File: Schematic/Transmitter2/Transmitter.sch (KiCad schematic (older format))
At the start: 50 parts, among them J1 Conn_01x06, J2 Antenna, J3 Conn_01x01, Q1 MMBT3904, Q2 MMBT3904, Q3 MMBT3904, U1 SN74HCU04N, U2 MH-M18, U3 SN74LS74AN, U4 LF351D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

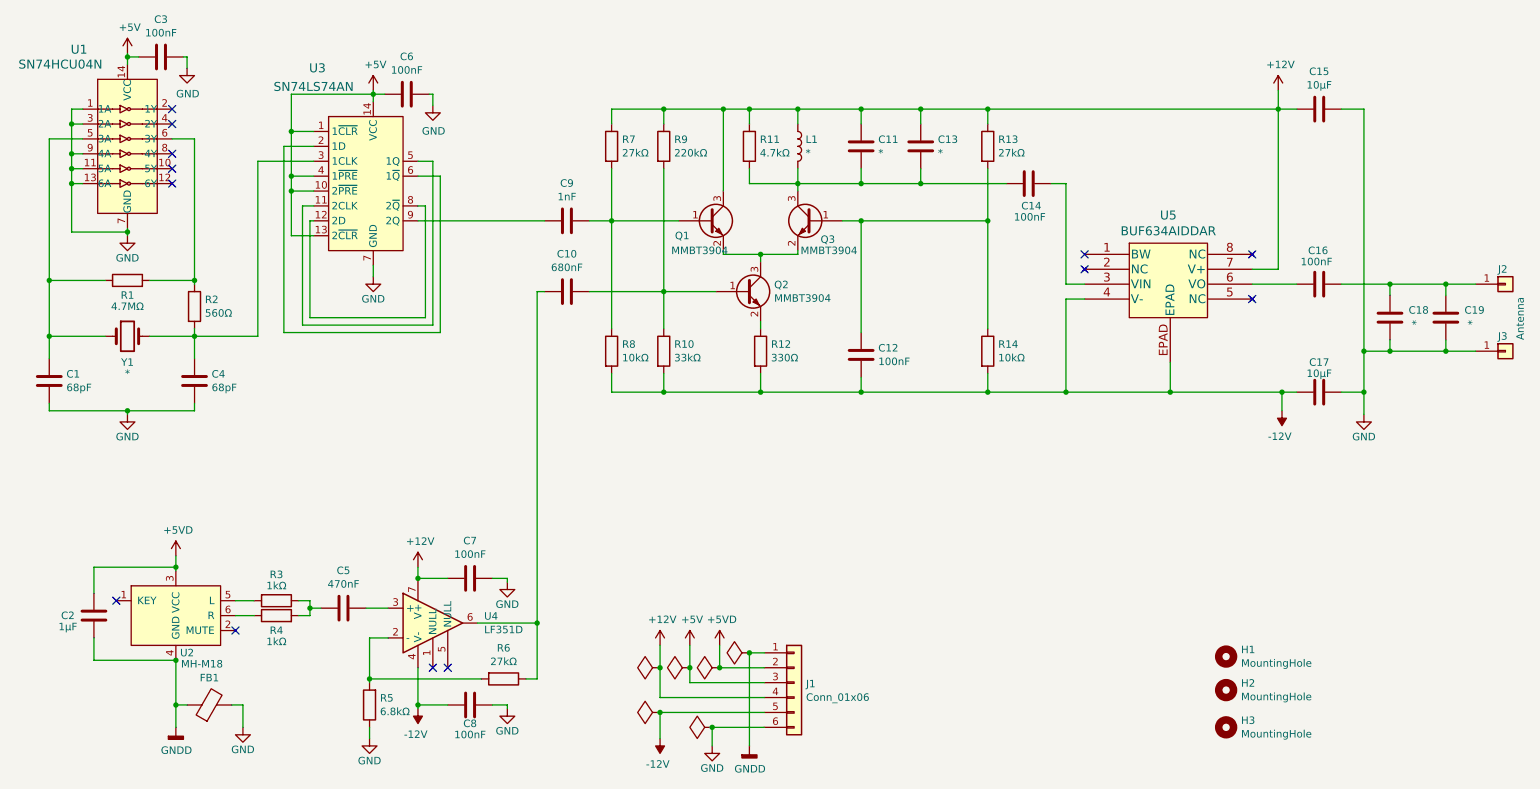
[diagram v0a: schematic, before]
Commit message: Added missing resistor: R15
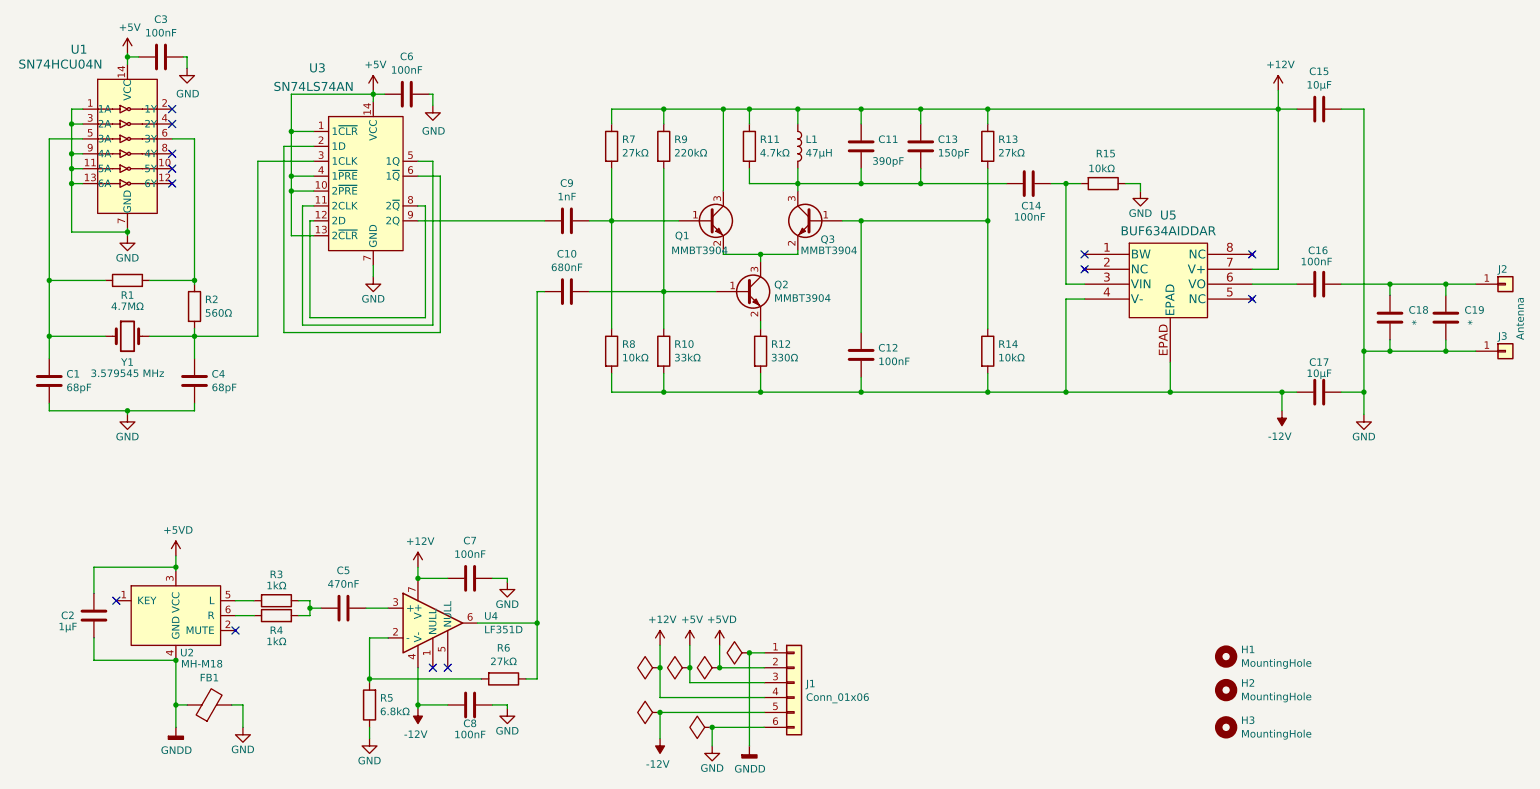
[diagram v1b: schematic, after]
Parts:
- added R15: 10kΩ, Resistor_SMD:R_0603_1608Metric_Pad1.05x0.95mm_HandSolder, symbol Device:R
- C11: value * -> 390pF
- C13: value * -> 150pF
- L1: value * -> 47µH; footprint Inductor_SMD:L_0603_1608Metric_Pad1.05x0.95mm_HandSolder -> Inductor_SMD:L_0805_2012Metric_Pad1.15x1.40mm_HandSolder
- Y1: value * -> 3.579545 MHz
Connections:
- net GND: now also R15.1
- net at C14.1, U5.3 (VIN): now also R15.2
